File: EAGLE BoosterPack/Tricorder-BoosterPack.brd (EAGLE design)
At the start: 63.5 x 34.3 mm, 27 parts, among them U1 MAG3110, U2 LMT70LMT70

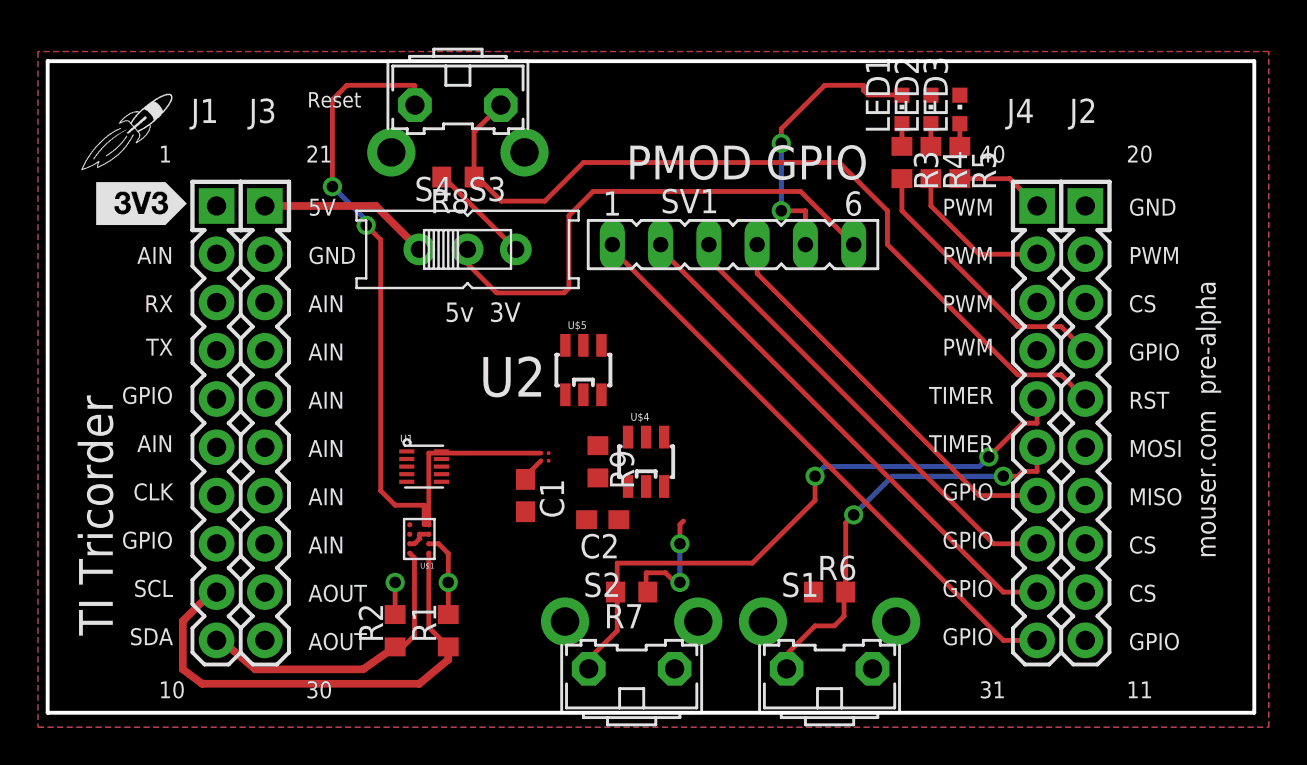
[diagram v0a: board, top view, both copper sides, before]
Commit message: Hardware Lock
Hardware design locked for TI review and approval.  3D CAD files
updated to reflect new PCB dimensions.
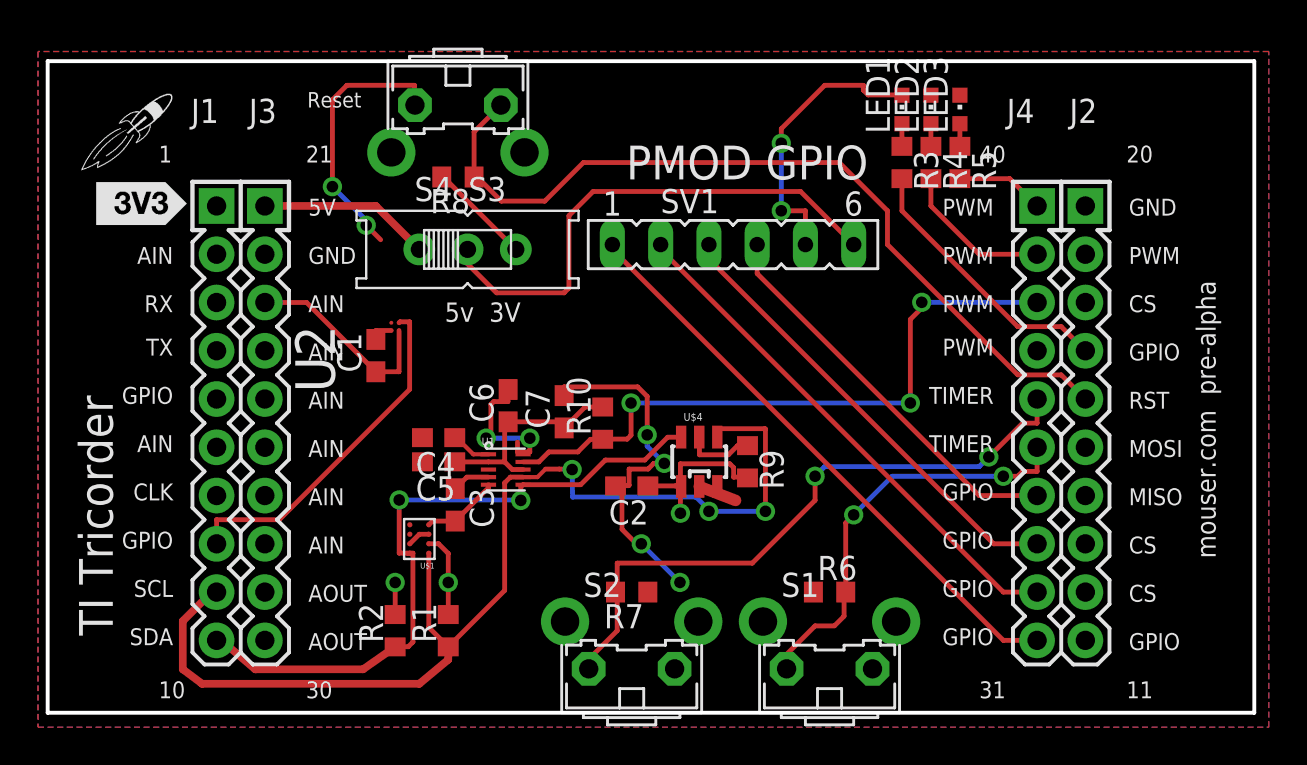
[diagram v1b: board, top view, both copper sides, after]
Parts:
- removed U$5: TPL5010, LPT5010:TPL5010
- added C3, C4, C5, C7: 100n, adafruit:C0603
- added C6: 1u, adafruit:C0603
- added R10: 10k, resistor:R0603
- moved C1 10.8 mm to (17.3, 18.8), turned to 90 degrees
- moved U2 10.4 mm to (18.3, 20.3), turned to 90 degrees
- moved R9 7.87 mm to (36.8, 13.2)
- moved U1 4.30 mm to (24.1, 12.8)
- moved U$4 2.79 mm to (34.3, 13.2)
- moved C2 2.34 mm to (30.7, 11.9)
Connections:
- removed net BKLT: A1.8
- removed net LCD_RST: A1.11
- new net N$11: C5.1, C6.1, C7.1, R10.2, U1.2, U1.8
- new net N$8: C3.1, U1.4
- new net N$9: C4.1, U1.1
- net GND: now also C3.2, C4.2, C5.2, C6.2, C7.2, U1.10, U1.5; no longer U$5.2
- net LCD_CS: now also A1.6; no longer A1.13
- net LMT_TON: now also A1.8; no longer A1.37
- net MAG_INT: now also R10.1, U1.9
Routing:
- net MAG_INT: track 0.00 -> 34.3 mm, vias 0 -> 3
- net SCL: track 25.7 -> 58.6 mm, vias 0 -> 3
- net SDA: track 16.0 -> 36.3 mm, vias 0 -> 2
- net LMT_TON: track 0.00 -> 18.4 mm
- net N$11: track 0.00 -> 11.5 mm
- net LMT_TAO: track 1.32 -> 10.7 mm
- net 3V: track 11.7 -> 20.6 mm, vias 2 -> 3
- net N$5: track 0.00 -> 4.13 mm
- net N$9: track 0.00 -> 2.14 mm
- net N$8: track 0.00 -> 2.00 mm
- net GND: track 63.7 -> 64.7 mm, vias 6 -> 10

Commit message: LMP91000 and Alphasense O2-A1 Sensor
Reconfigured board to include a TI LMP91000 gas sensor I2C interface
chip and placeholder for Alphasense O2-A1 oxygen sensor
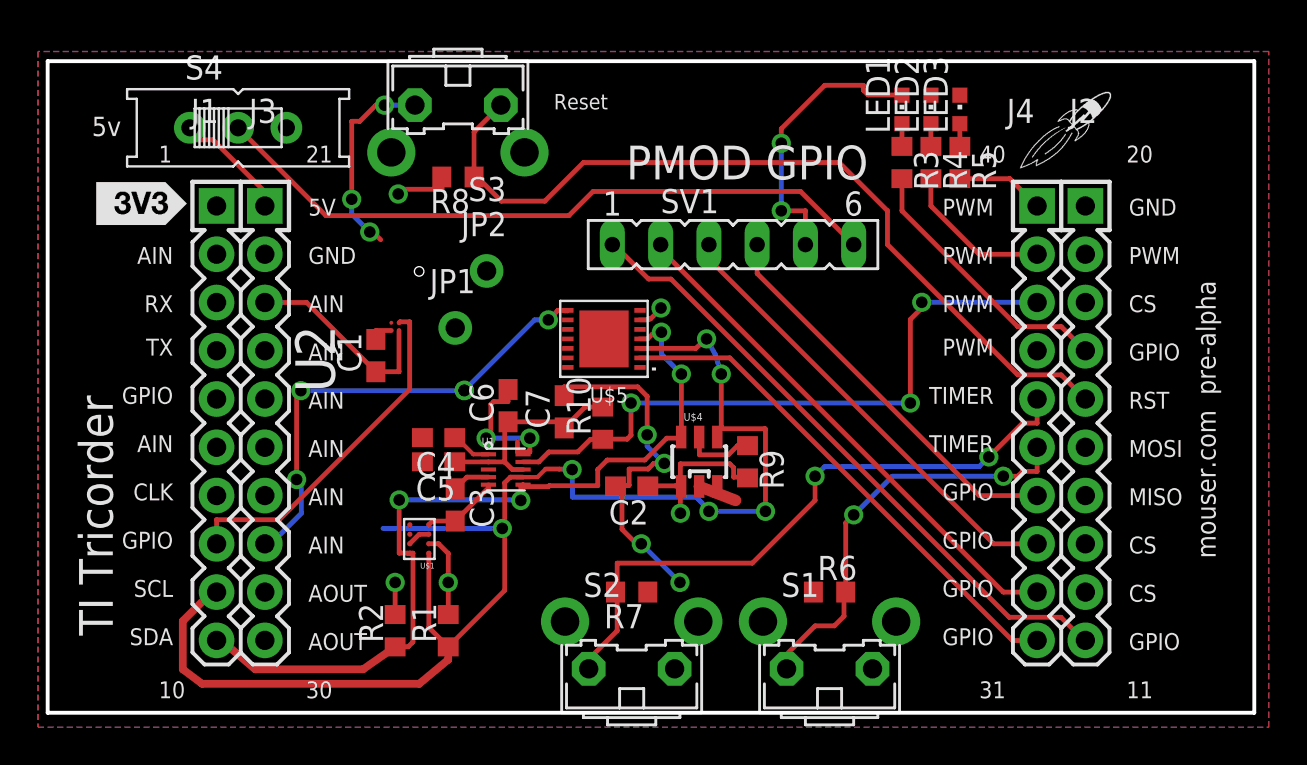
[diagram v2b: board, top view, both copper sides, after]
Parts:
- added JP1, JP2: (no value), adafruit:1X01-CLEANBIG
- added U$5: LMP91000, LMP91000:WFDFN-14
- moved U$2 49.4 mm to (53.7, 30.8)
- moved S4 13.7 mm to (10.0, 30.8)
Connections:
- new net LMP91000_MENB: A1.31, U$5.2
- new net LMP91000_VOUT: A1.28, U$5.8
- new net VE_NEG: JP1.1, U$5.13, U$5.14
- new net VE_POS: JP2.1, U$5.12
- new net VREF: U$5.11
- net 3V: now also U$5.6
- net GND: now also U$5.1, U$5.7
- net IO1: now also A1.11; no longer A1.31
- net SCL: now also U$5.3
- net SDA: now also U$5.4
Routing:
- net LMP91000_MENB: track 0.00 -> 27.1 mm
- net LMP91000_VOUT: track 0.00 -> 25.3 mm, vias 0 -> 5
- net SCL: track 58.6 -> 74.4 mm, vias 3 -> 6
- net N$4: track 27.3 -> 36.0 mm
- net SDA: track 36.3 -> 44.1 mm, vias 2 -> 4
- net GND: track 64.7 -> 61.7 mm, vias 10 -> 11
- net 5V: track 9.07 -> 6.48 mm
- net IO1: track 31.1 -> 33.5 mm
- net 3V: track 20.6 -> 19.7 mm, vias 3 -> 5
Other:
- board text added: "5v"
- board text removed: "5v 3V"

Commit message: O2 Sensor Moved Offboard
Replace onboard O2 sensor with header pins to allow for off board
placement of sensor. Eagle files revised as well as documentation files.
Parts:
- removed JP2: (no value), adafruit:1X01-CLEANBIG
- added R11: 0, resistor:R0603
- JP1: device adafruit:1X01-CLEANBIG -> adafruit:1X03-CLEANBIG
- moved JP1 2.85 mm to (21.4, 23.1)
- renumbered U$1 to U3, U$4 to U4, U$5 to U5
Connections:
- removed net VE_NEG: JP1.1, U5.13, U5.14
- removed net VE_POS: JP2.1, U5.12
- new net CE: JP1.1, R11.1, U5.14
- new net RE: JP1.2, R11.2, U5.13
- new net WE: JP1.3, U5.12
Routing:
- net CE: track 0.00 -> 11.6 mm
- net RE: track 0.00 -> 9.34 mm
- net WE: track 0.00 -> 6.42 mm
